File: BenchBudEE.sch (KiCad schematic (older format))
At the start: 0 parts

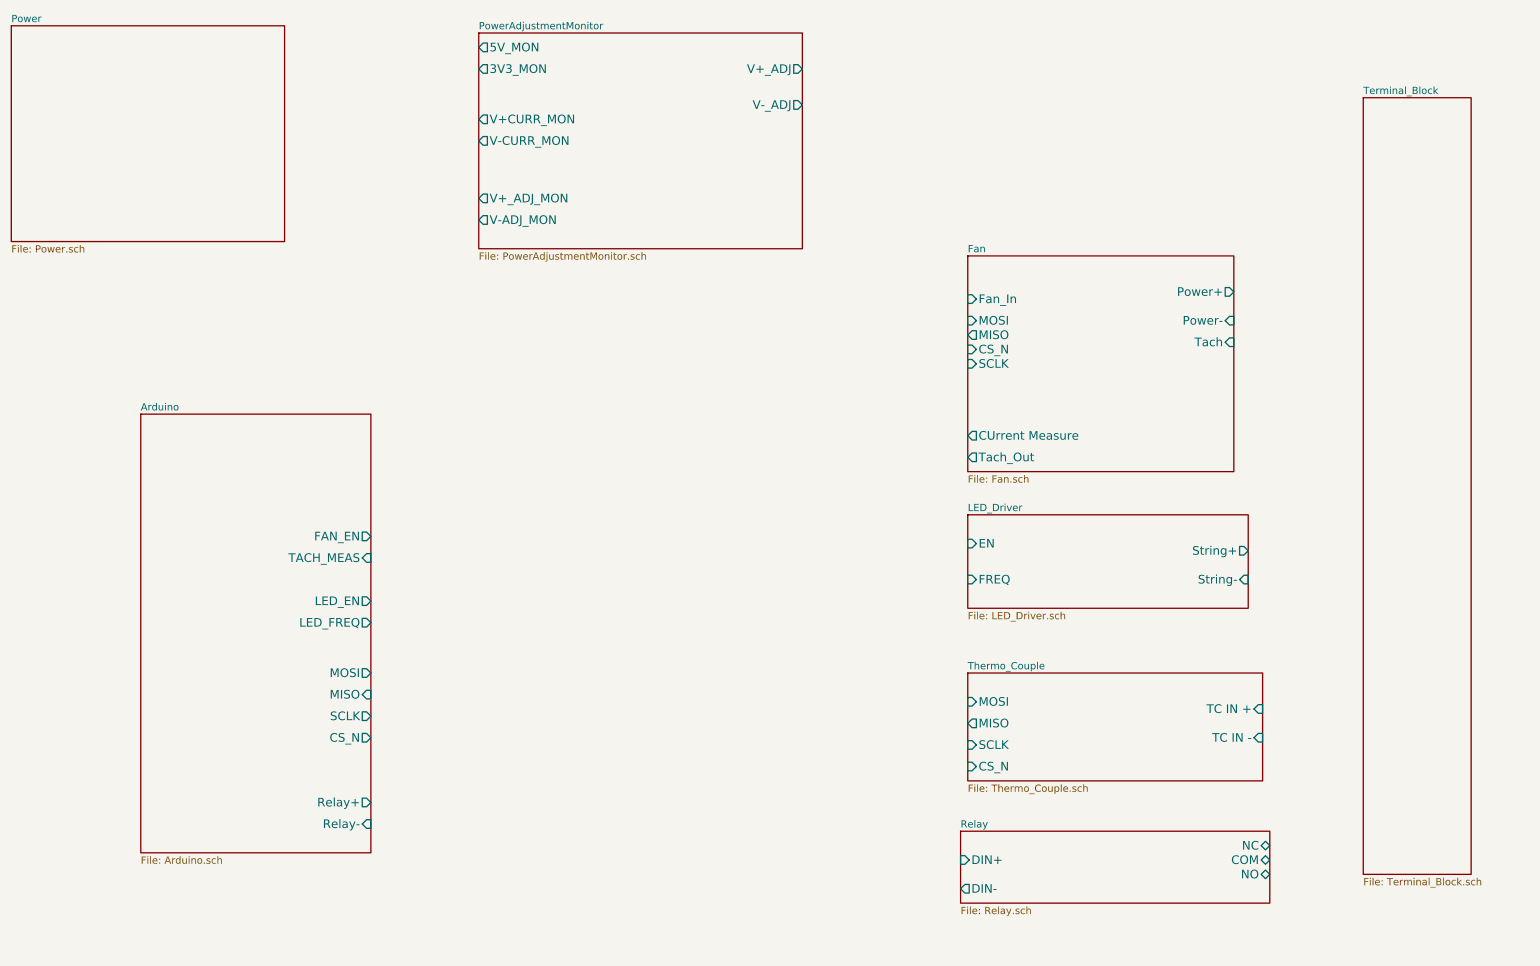
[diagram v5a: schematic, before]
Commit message: Create Arduino Schematic and Wire Up top Level
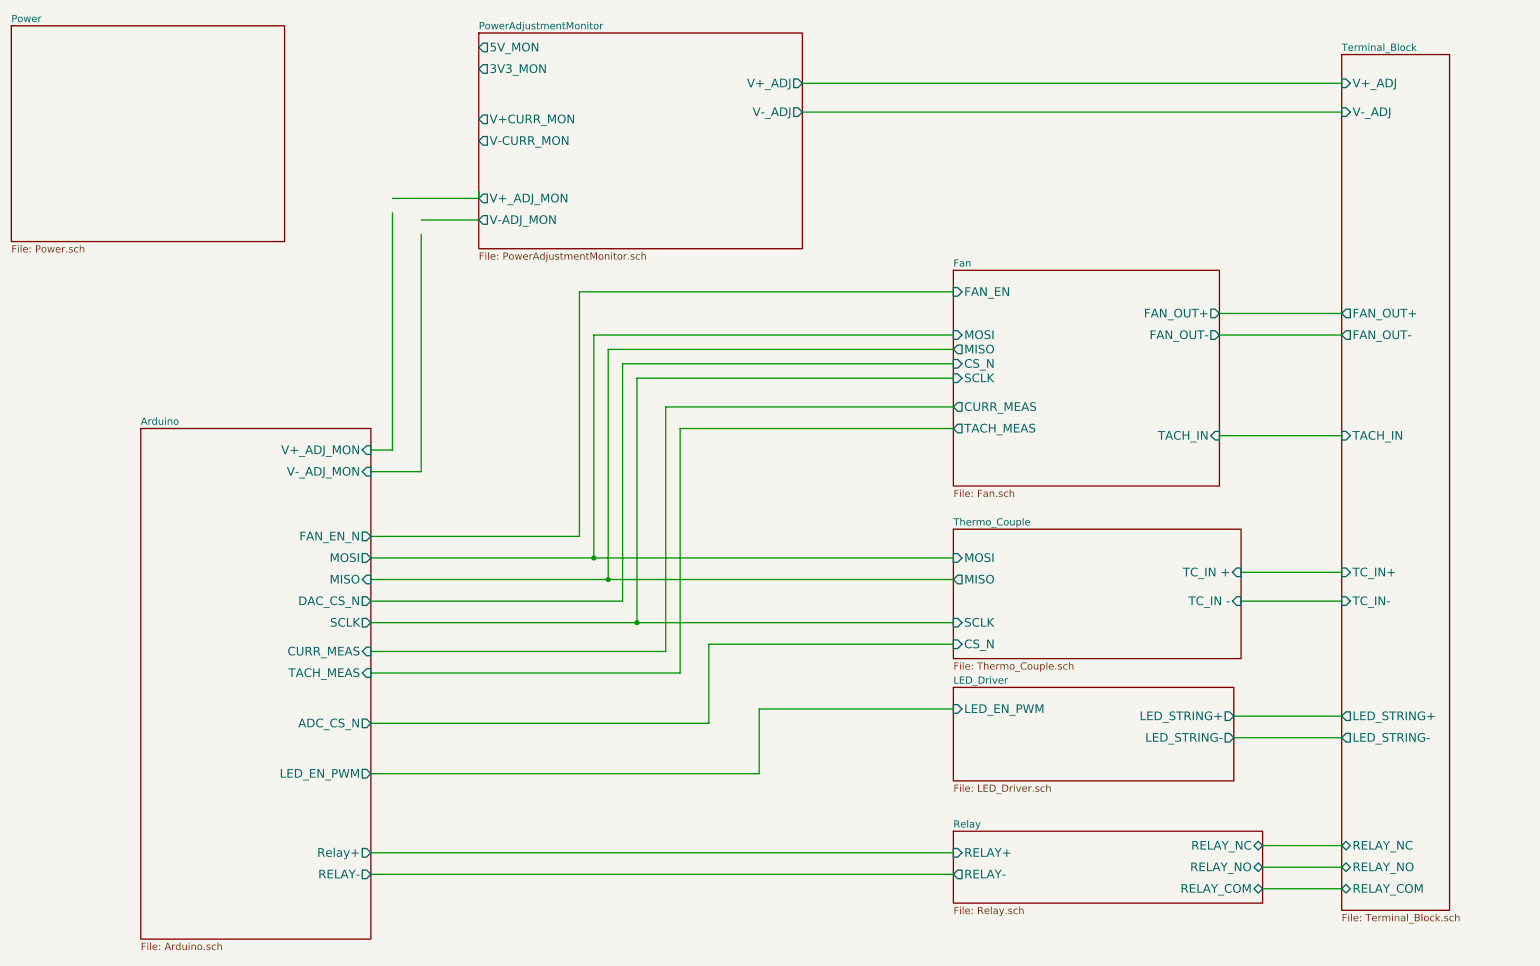
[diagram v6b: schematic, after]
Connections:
- wire segments 0 -> 48
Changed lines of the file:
@@
 $EndDescr
 $Sheet
-S 1650 3450 1600 3050
+S 1650 3550 1600 3550
 U 52EECD1D
 F0 "Arduino" 50
 F1 "Arduino.sch" 50
-F2 "Relay+" O R 3250 6150 60
-F3 "Relay-" I R 3250 6300 60
-F4 "MOSI" O R 3250 5250 60
-F5 "MISO" I R 3250 5400 60
-F6 "SCLK" O R 3250 5550 60
-F7 "CS_N" O R 3250 5700 60
-F8 "LED_EN" O R 3250 4750 60
-F9 "LED_FREQ" O R 3250 4900 60
-F10 "FAN_EN" O R 3250 4300 60
-F11 "TACH_MEAS" I R 3250 4450 60
-$EndSheet
-$Sheet
-S 7350 6350 2150 500
-U 52EECD80
-F0 "Relay" 50
-F1 "Relay.sch" 50
-F2 "DIN+" I L 7350 6550 60
-F3 "DIN-" O L 7350 6750 60
-F4 "NC" B R 9500 6450 60
-F5 "NO" B R 9500 6650 60
-F6 "COM" B R 9500 6550 60
+F2 "Relay+" O R 3250 6500 60
+F3 "MOSI" O R 3250 4450 60
+F4 "MISO" I R 3250 4600 60
+F5 "SCLK" O R 3250 4900 60
+F6 "TACH_MEAS" I R 3250 5250 60
+F7 "RELAY-" O R 3250 6650 60
+F8 "FAN_EN_N" O R 3250 4300 60
+F9 "CURR_MEAS" I R 3250 5100 60
+F10 "V+_ADJ_MON" I R 3250 3700 60
+F11 "V-_ADJ_MON" I R 3250 3850 60
+F12 "LED_EN_PWM" O R 3250 5950 60
+F13 "DAC_CS_N" O R 3250 4750 60
+F14 "ADC_CS_N" O R 3250 5600 60
 $EndSheet
 $Sheet
@@
 $EndSheet
 $Sheet
-S 7400 4150 1950 650
+S 7300 5350 1950 650
 U 52EECDCB
 F0 "LED_Driver" 50
 F1 "LED_Driver.sch" 50
-F2 "EN" I L 7400 4350 60
-F3 "FREQ" I L 7400 4600 60
-F4 "String+" O R 9350 4400 60
-F5 "String-" I R 9350 4600 60
-$EndSheet
-$Sheet
-S 7400 2350 1850 1500
+F2 "LED_EN_PWM" I L 7300 5500 60
+F3 "LED_STRING+" O R 9250 5550 60
+F4 "LED_STRING-" O R 9250 5700 60
+$EndSheet
+$Sheet
+S 7300 2450 1850 1500
 U 52EECDEA
 F0 "Fan" 50
 F1 "Fan.sch" 50
-F2 "Power+" O R 9250 2600 60
-F3 "Power-" I R 9250 2800 60
-F4 "Tach" I R 9250 2950 60
-F5 "Tach_Out" O L 7400 3750 60
-F6 "Fan_In" I L 7400 2650 60
-F7 "CUrrent Measure" O L 7400 3600 60
-F8 "MOSI" I L 7400 2800 60
-F9 "MISO" O L 7400 2900 60
-F10 "CS_N" I L 7400 3000 60
-F11 "SCLK" I L 7400 3100 60
-$EndSheet
-$Sheet
-S 10150 1250 750  5400
-U 52EECE17
-F0 "Terminal_Block" 50
-F1 "Terminal_Block.sch" 50
-$EndSheet
-$Sheet
-S 7400 5250 2050 750
-U 52EECD62
-F0 "Thermo_Couple" 50
-F1 "Thermo_Couple.sch" 50
-F2 "TC IN +" I R 9450 5500 60
-F3 "TC IN -" I R 9450 5700 60
-F4 "MISO" O L 7400 5600 60
-F5 "SCLK" I L 7400 5750 60
-F6 "CS_N" I L 7400 5900 60
-F7 "MOSI" I L 7400 5450 60
+F2 "MOSI" I L 7300 2900 60
+F3 "MISO" O L 7300 3000 60
+F4 "CS_N" I L 7300 3100 60
+F5 "SCLK" I L 7300 3200 60
+F6 "FAN_OUT+" O R 9150 2750 60
+F7 "TACH_IN" I R 9150 3600 60
+F8 "TACH_MEAS" O L 7300 3550 60
+F9 "FAN_EN" I L 7300 2600 60
+F10 "CURR_MEAS" O L 7300 3400 60
+F11 "FAN_OUT-" O R 9150 2900 60
 $EndSheet
 $Sheet
@@
 F0 "PowerAdjustmentMonitor" 50
 F1 "PowerAdjustmentMonitor.sch" 50
-F2 "V+_ADJ" O R 6250 1050 60
-F3 "V-_ADJ" O R 6250 1300 60
+F2 "V+_ADJ" O R 6250 1150 60
+F3 "V-_ADJ" O R 6250 1350 60
 F4 "3V3_MON" O L 4000 1050 60
 F5 "5V_MON" O L 4000 900 60
@@
 F9 "V-CURR_MON" O L 4000 1550 60
 $EndSheet
+Wire Wire Line
+	9450 6450 10000 6450
+Wire Wire Line
+	10000 6600 9450 6600
+Wire Wire Line
+	9450 6750 10000 6750
+Wire Wire Line
+	6250 1150 10000 1150
+Wire Wire Line
+	10000 1350 6250 1350
+Wire Wire Line
+	4000 1900 4000 1950
+Wire Wire Line
+	4000 1950 3400 1950
+Wire Wire Line
+	3400 2050 3400 3700
+Wire Wire Line
+	3400 3700 3250 3700
+Wire Wire Line
+	3250 3850 3600 3850
+Wire Wire Line
+	3600 3850 3600 2200
+Wire Wire Line
+	3600 2100 4000 2100
+$Sheet
+S 7300 4250 2000 900
+U 52EECD62
+F0 "Thermo_Couple" 50
+F1 "Thermo_Couple.sch" 50
+F2 "MISO" O L 7300 4600 60
+F3 "SCLK" I L 7300 4900 60
+F4 "CS_N" I L 7300 5050 60
+F5 "MOSI" I L 7300 4450 60
+F6 "TC_IN +" I R 9300 4550 60
+F7 "TC_IN -" I R 9300 4750 60
+$EndSheet
+$Sheet
+S 7300 6350 2150 500
+U 52EECD80
+F0 "Relay" 50
+F1 "Relay.sch" 50
+F2 "RELAY_NC" B R 9450 6450 60
+F3 "RELAY_NO" B R 9450 6600 60
+F4 "RELAY_COM" B R 9450 6750 60
+F5 "RELAY+" I L 7300 6500 60
+F6 "RELAY-" O L 7300 6650 60
+$EndSheet
+$Sheet
+S 10000 950  750  5950
+U 52EECE17
+F0 "Terminal_Block" 50
+F1 "Terminal_Block.sch" 50
+F2 "V+_ADJ" I L 10000 1150 60
+F3 "V-_ADJ" I L 10000 1350 60
+F4 "FAN_OUT+" O L 10000 2750 60
+F5 "FAN_OUT-" O L 10000 2900 60
+F6 "TACH_IN" I L 10000 3600 60
+F7 "LED_STRING+" O L 10000 5550 60
+F8 "LED_STRING-" O L 10000 5700 60
+F9 "TC_IN+" I L 10000 4550 60
+F10 "TC_IN-" I L 10000 4750 60
+F11 "RELAY_NC" B L 10000 6450 60
+F12 "RELAY_NO" B L 10000 6600 60
+F13 "RELAY_COM" B L 10000 6750 60
+$EndSheet
+Wire Wire Line
+	7300 2600 4700 2600
+Wire Wire Line
+	4700 2600 4700 4300
+Wire Wire Line
+	4700 4300 3250 4300
+Wire Wire Line
+	4800 2900 4800 4450
+Wire Wire Line
+	4800 2900 7300 2900
+Wire Wire Line
+	3250 4450 7300 4450
+Wire Wire Line
+	3250 4600 7300 4600
+Wire Wire Line
+	4900 3000 4900 4600
+Wire Wire Line
+	4900 3000 7300 3000
+Wire Wire Line
+	5000 4750 3250 4750
+Wire Wire Line
+	5000 3100 5000 4750
+Wire Wire Line
+	5000 3100 7300 3100
+Wire Wire Line
+	7300 3200 5100 3200
+Wire Wire Line
+	5100 3200 5100 4900
+Wire Wire Line
+	3250 4900 7300 4900
+Wire Wire Line
+	5300 5100 3250 5100
+Wire Wire Line
+	5300 3400 5300 5100
+Wire Wire Line
+	5300 3400 7300 3400
+Wire Wire Line
+	7300 3550 5400 3550
+Wire Wire Line
+	5400 3550 5400 5250
+Wire Wire Line
+	5400 5250 3250 5250
+Connection ~ 4800 4450
+Connection ~ 4900 4600
+Connection ~ 5100 4900
+Wire Wire Line
+	3250 5600 5600 5600
+Wire Wire Line
+	5600 5600 5600 5050
+Wire Wire Line
+	5600 5050 7300 5050
+Wire Wire Line
+	7300 5500 5950 5500
+Wire Wire Line
+	5950 5500 5950 5950
+Wire Wire Line
+	5950 5950 3250 5950
+Wire Wire Line
+	3250 6500 7300 6500
+Wire Wire Line
+	7300 6650 3250 6650
+Wire Wire Line
+	9300 4550 10000 4550
+Wire Wire Line
+	10000 4750 9300 4750
+Wire Wire Line
+	10000 3600 9150 3600
+Wire Wire Line
+	10000 2900 9150 2900
+Wire Wire Line
+	9150 2750 10000 2750
+Wire Wire Line
+	9250 5550 10000 5550
+Wire Wire Line
+	9250 5700 10000 5700
 $EndSCHEMATC

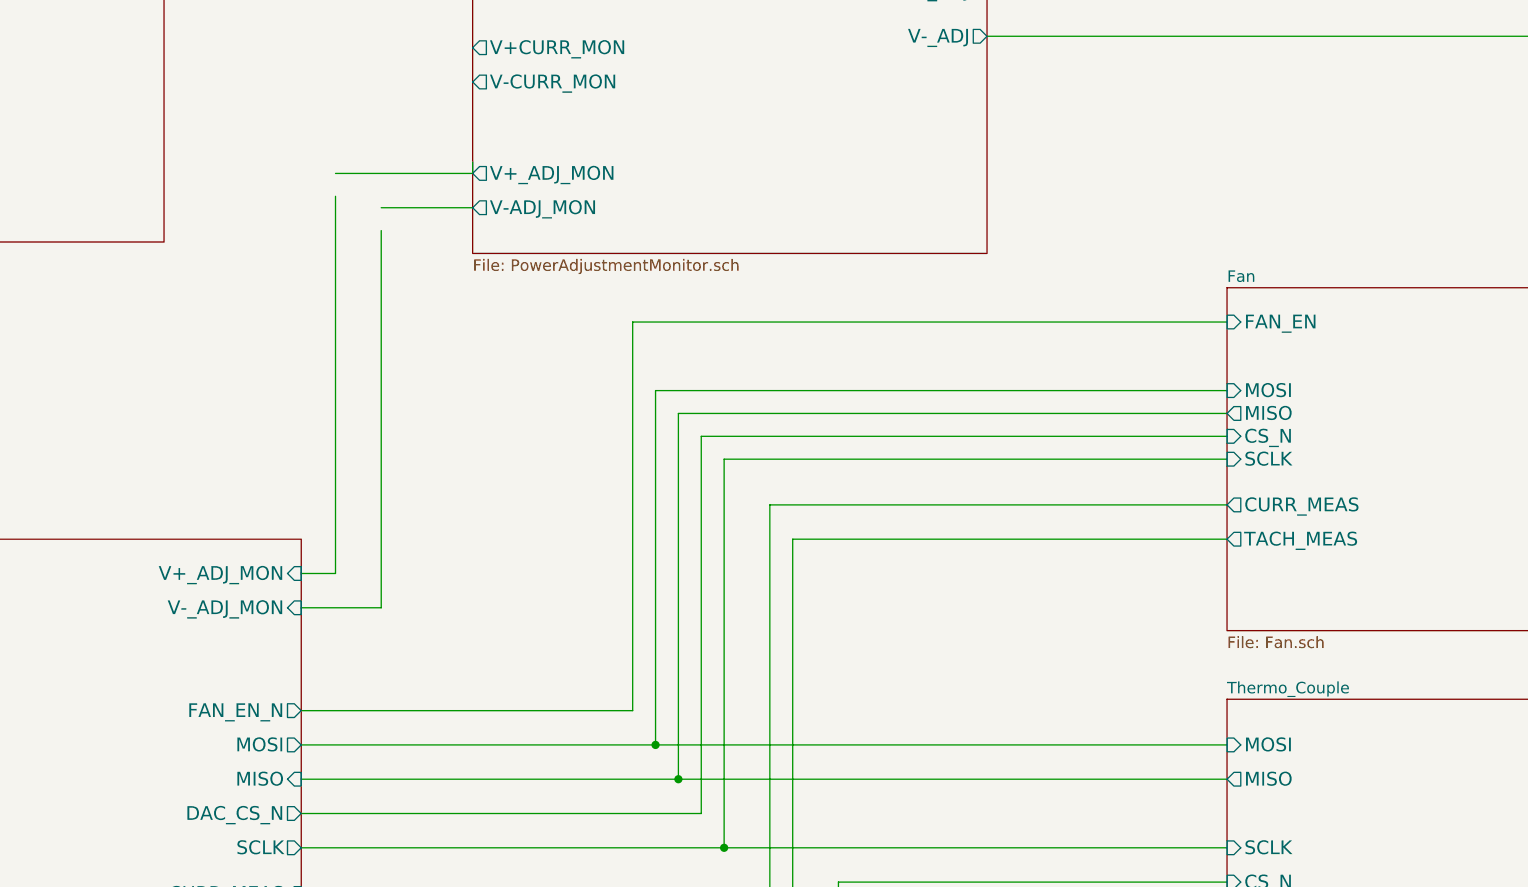
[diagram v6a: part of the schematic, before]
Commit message: Upgrade Current/Fan Output Schem Use PWM
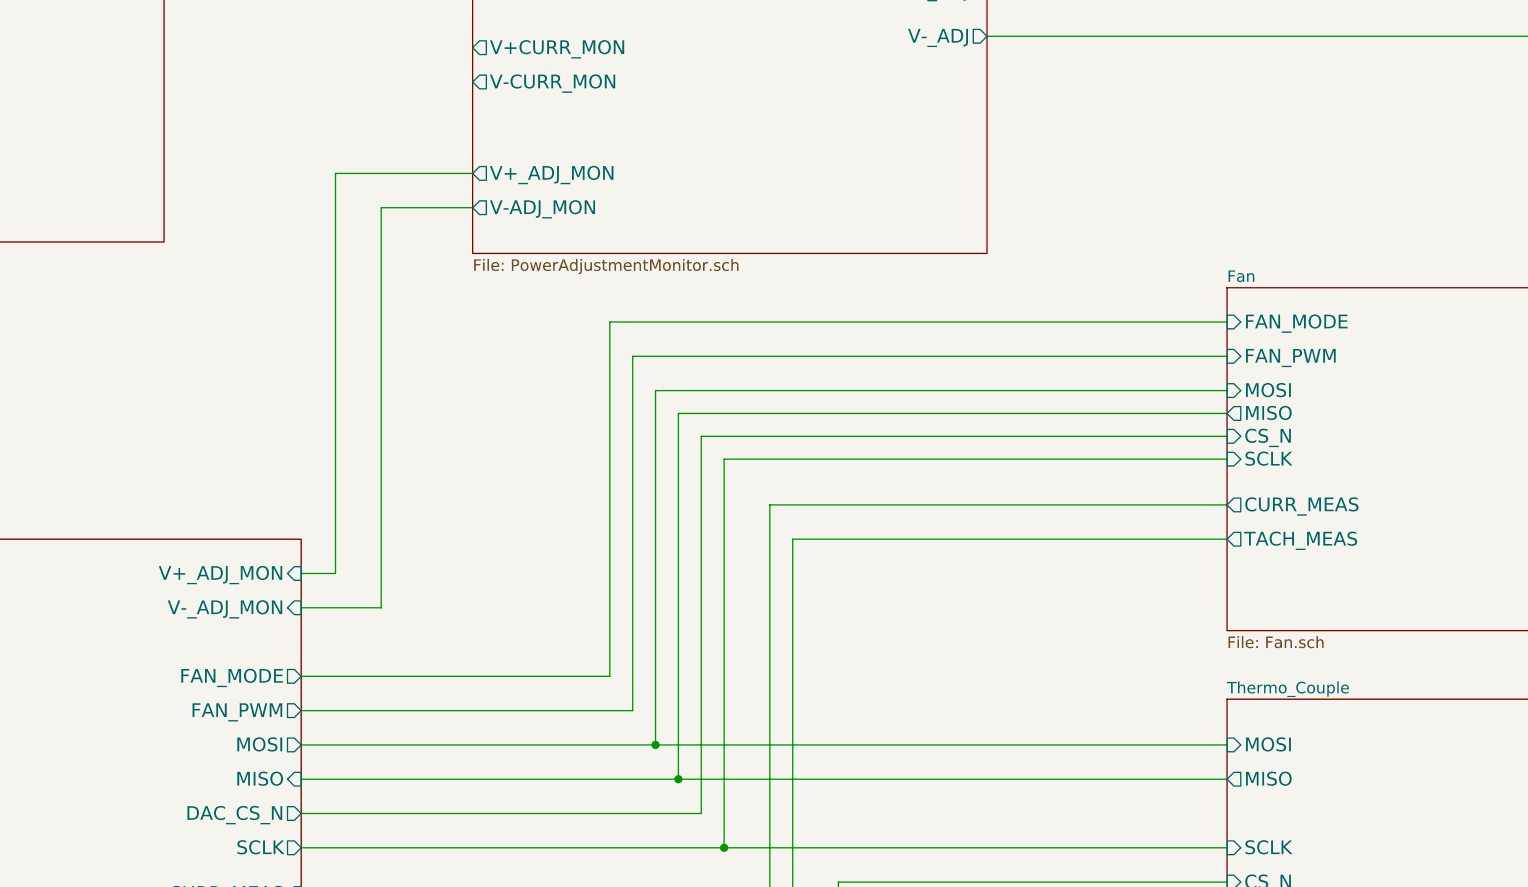
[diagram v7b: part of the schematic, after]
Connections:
- wire segments 48 -> 50
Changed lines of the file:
@@
 Sheet 1 9
 Title ""
-Date "5 feb 2014"
+Date "9 feb 2014"
 Rev ""
 Comp ""
@@
 F6 "TACH_MEAS" I R 3250 5250 60
 F7 "RELAY-" O R 3250 6650 60
-F8 "FAN_EN_N" O R 3250 4300 60
-F9 "CURR_MEAS" I R 3250 5100 60
-F10 "V+_ADJ_MON" I R 3250 3700 60
-F11 "V-_ADJ_MON" I R 3250 3850 60
-F12 "LED_EN_PWM" O R 3250 5950 60
-F13 "DAC_CS_N" O R 3250 4750 60
-F14 "ADC_CS_N" O R 3250 5600 60
+F8 "CURR_MEAS" I R 3250 5100 60
+F9 "V+_ADJ_MON" I R 3250 3700 60
+F10 "V-_ADJ_MON" I R 3250 3850 60
+F11 "LED_EN_PWM" O R 3250 5950 60
+F12 "DAC_CS_N" O R 3250 4750 60
+F13 "ADC_CS_N" O R 3250 5600 60
+F14 "FAN_PWM" O R 3250 4300 60
+F15 "FAN_MODE" O R 3250 4150 60
 $EndSheet
 $Sheet
@@
 F7 "TACH_IN" I R 9150 3600 60
 F8 "TACH_MEAS" O L 7300 3550 60
-F9 "FAN_EN" I L 7300 2600 60
-F10 "CURR_MEAS" O L 7300 3400 60
-F11 "FAN_OUT-" O R 9150 2900 60
+F9 "CURR_MEAS" O L 7300 3400 60
+F10 "FAN_OUT-" O R 9150 2900 60
+F11 "FAN_PWM" I L 7300 2750 60
+F12 "FAN_MODE" I L 7300 2600 60
 $EndSheet
 $Sheet
@@
 	10000 1350 6250 1350
 Wire Wire Line
-	4000 1900 4000 1950
-Wire Wire Line
 	4000 1950 3400 1950
 Wire Wire Line
-	3400 2050 3400 3700
+	3400 1950 3400 3700
 Wire Wire Line
 	3400 3700 3250 3700
 Wire Wire Line
-	3250 3850 3600 3850
-Wire Wire Line
-	3600 3850 3600 2200
+	3600 3850 3250 3850
+Wire Wire Line
+	3600 2100 3600 3850
 Wire Wire Line
 	3600 2100 4000 2100
@@
 $EndSheet
 Wire Wire Line
-	7300 2600 4700 2600
-Wire Wire Line
-	4700 2600 4700 4300
+	7300 2750 4700 2750
+Wire Wire Line
+	4700 2750 4700 4300
 Wire Wire Line
 	4700 4300 3250 4300
@@
 Wire Wire Line
 	9250 5700 10000 5700
+Wire Wire Line
+	3250 4150 4600 4150
+Wire Wire Line
+	4600 4150 4600 2600
+Wire Wire Line
+	4600 2600 7300 2600
 $EndSCHEMATC
